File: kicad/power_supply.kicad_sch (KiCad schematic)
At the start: 14 parts, among them U2 LMR16030

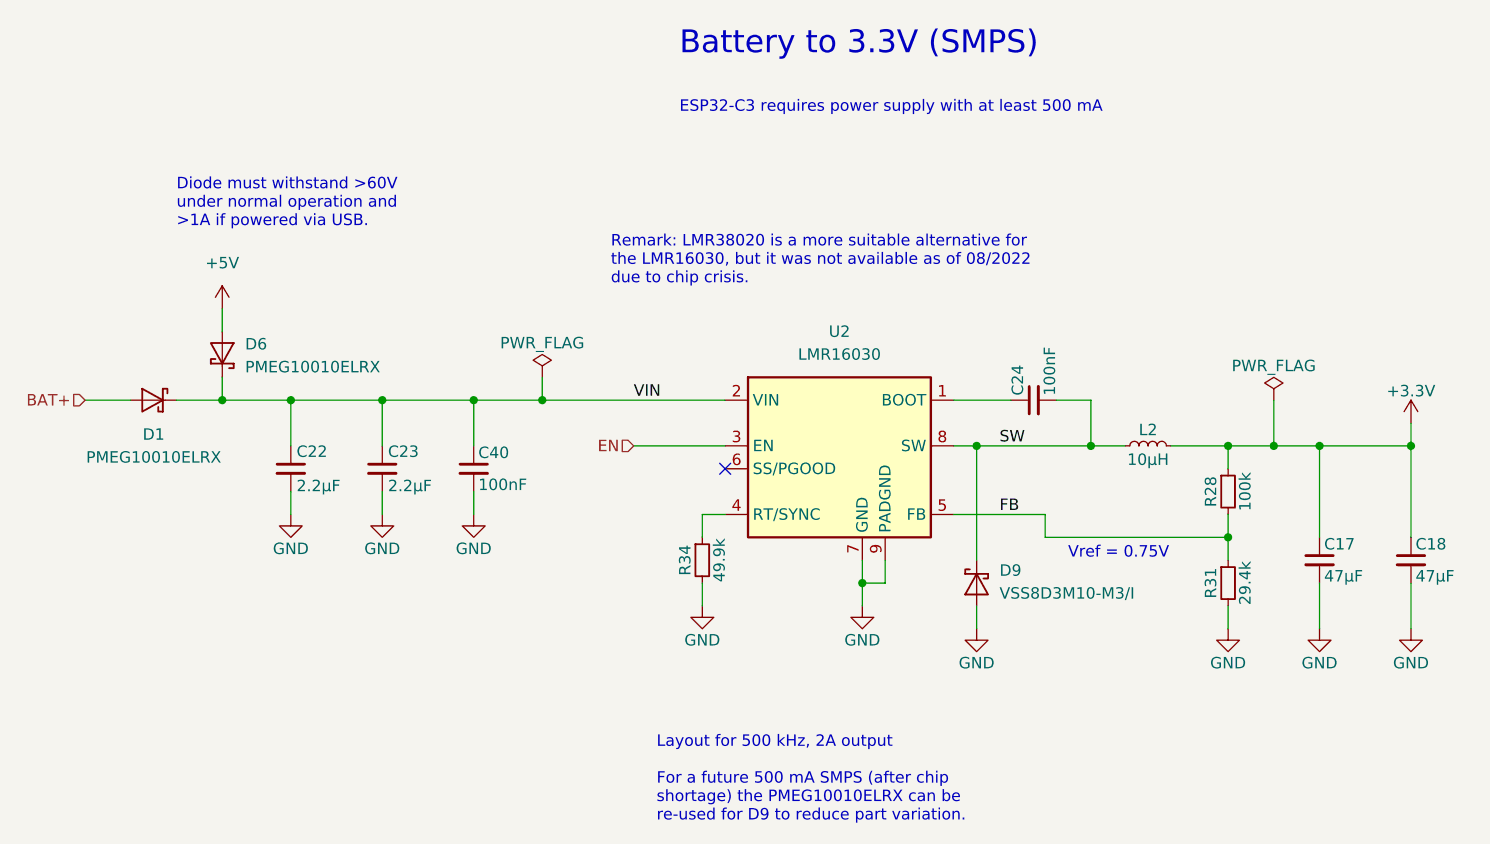
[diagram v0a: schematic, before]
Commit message: v0.4.0: Multiple improvements for new board revision
- Use LMR38010 for internal power supply (max. 80V instead of 60V)
- Change USB connector from Micro-A to C and remove 5V power supply
  which was not working anyway. The board cannot be powered by USB
  only.
- Add TS2 (connected to DFETOFF) to measure shunt temperature
- Add RS-485 transceiver (sharing the connector with CAN)
- Switch I2C pins of ESP32-C3 to GPIO8/9. This allows to re-use the
  I2C pull-ups for strapping configuration and frees two pins for the
  RS-485 transceiver RE and DE pins. Also we may get rid of the I2C
  glitches during start-up.
- Use 80V instead of 100V power MOSFETs to reduce Rds(on).
- Reduce DSG gate resistor R57 to 47R to increase switch-off speed.
- Adjust some resistors to reduce number of different parts
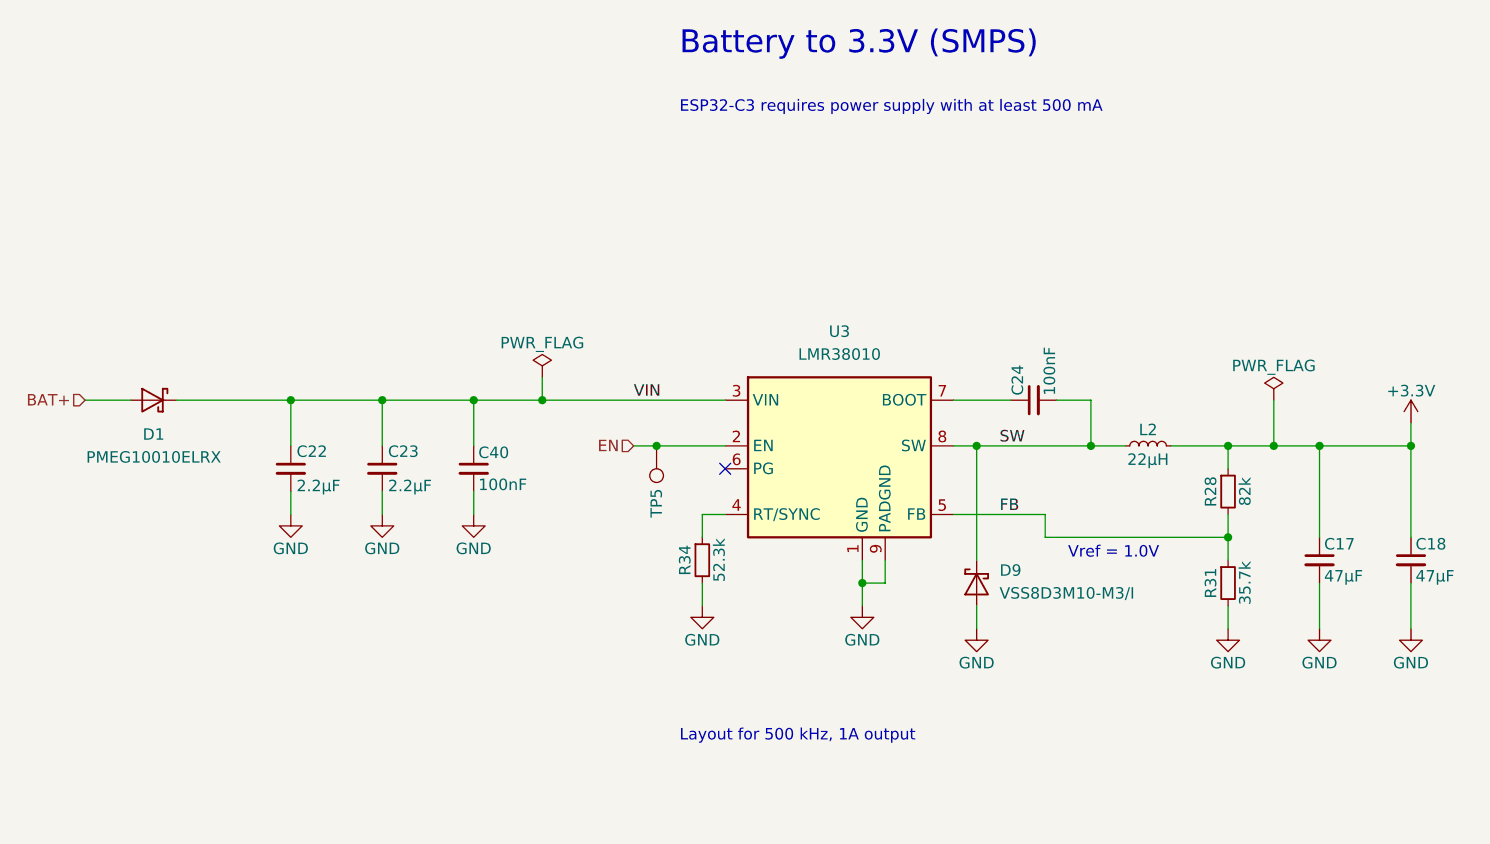
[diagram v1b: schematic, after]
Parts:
- removed D6: PMEG10010ELRX, LibreSolar:D_SOD-123F, symbol LibreSolar:D_Schottky
- removed U2: LMR16030, Package_SO:SOIC-8-1EP_3.9x4.9mm_P1.27mm_EP2.29x3mm, symbol LibreSolar:LMR16030
- added TP5: TestPoint, TestPoint:TestPoint_Pad_D1.5mm, symbol Connector:TestPoint
- added U3: LMR38010, LibreSolar:SOIC-8-1EP_3.9x4.9mm_P1.27mm_EP2.4x3.1mm_ThermalVias, symbol LibreSolar:LMR38020
- C17, C18: LCSC (none) -> C525654; Manufacturer Samsung -> Samsung Electro-Mechanics; Remarks 10V, X5R -> min. 10V, X5R
- C22, C23: LCSC (none) -> C55151; Manufacturer any -> Samsung Electro-Mechanics; PartNumber (none) -> CL32B225KCJSNNE; Remarks 100V, X7R -> min. 100V, X5R
- C24, C40: LCSC (none) -> C15725; Manufacturer any -> Samsung Electro-Mechanics; PartNumber (none) -> CL10B104KC8NNNC; Remarks X7R, 100V -> min. 100V, X7R
- D1: LCSC (none) -> C179426
- D9: LCSC (none) -> C3760174; PartNumber VSS8D3M10-M3/I -> VSS8D3M10-M3/H
- L2: value 10µH -> 22µH; LCSC (none) -> C92946; Manufacturer Tayo Yuden -> Bourns; PartNumber NR8040T100M -> SRN8040-220M; Remarks Alternative: Bourns SRN8040TA-100M -> Alternative: Tayo Yuden NR8040T220M
- R28: value 100k -> 82k; Manufacturer any -> Yageo; PartNumber (none) -> RC0603FR-0782KL; Remarks 1% -> (none)
- R31: value 29.4k -> 35.7k; Manufacturer any -> Yageo; PartNumber (none) -> RC0603FR-0735K7L; Remarks 1% -> (none)
- R34: value 49.9k -> 52.3k; Manufacturer any -> Yageo; PartNumber (none) -> RC0603FR-0752K3L; Remarks 1% -> (none)
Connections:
- net EN: now also TP5.1, U3.2 (EN)
- net FB: now also U3.5 (FB)
- net GND: now also U3.1 (GND), U3.9 (PADGND)
- net SW: now also U3.8 (SW)
- net VIN: now also U3.3 (VIN)
- net at C24.1: now also U3.7 (BOOT)
- net at R34.1: now also U3.4 (RT/SYNC)
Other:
- note added: "Layout for 500 kHz, 1A output"
- note added: "Vref = 1.0V"
- note removed: "Diode must withstand >60V under normal operation and >1A if powered via USB."
- note removed: "Layout for 500 kHz, 2A output For a future 500 mA SMPS (after chip shortage) the PMEG10010ELRX can be re-used for D9 to reduce part variation."
- note removed: "Remark: LMR38020 is a more suitable alternative for the LMR16030, but it was not available as of 08/2022 due to chip crisis."
- note removed: "Vref = 0.75V"

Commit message: Update files to KiCad v8
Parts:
- U3: LCSC (none) -> C3192337; Remarks (none) -> Alternative: LMR38020SDDAR

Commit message: Create cost-optimized Lite variant of the BMS C1 v0.4.1
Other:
- title: Libre Solar BMS C1 -> Libre Solar BMS C1 lite
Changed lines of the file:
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@@
 	(paper "A4")
 	(title_block
-		(title "Libre Solar BMS C1")
+		(title "Libre Solar BMS C1 lite")
 		(date "2024-03-17")
 		(rev "0.4.1")
